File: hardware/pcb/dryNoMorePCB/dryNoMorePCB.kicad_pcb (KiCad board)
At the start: 2 copper layers, 76.2 x 44.2 mm, 34 parts, among them J1 USB_A_Stacked, J10 Barrel_Jack_MountingPin, J11 Conn_01x03, J12 Conn_01x03, J13 Conn_02x06_Odd_Even, J2 Conn_01x03, J3 Conn_01x03, J4 Conn_01x03, J5 USB_A_Stacked, J6 Conn_01x03, J7 Conn_01x03, J8 Conn_01x03, J9 USB_A_Stacked, Q1 Q_NMOS_GDSD, Q2 Q_NMOS_GDSD, Q3 Q_NMOS_GDSD, Q4 Q_NMOS_GDSD, Q5 Q_NMOS_GDSD, Q6 Q_NMOS_GDSD, U1 74HC595, U2 74HC595

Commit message: more routing nightmares incoming
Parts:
- added J14: Conn_02x06_Odd_Even, Connector_PinSocket_2.54mm:PinSocket_2x06_P2.54mm_Horizontal, F.Cu at (77.7, 87.1)
- added J15: Conn_01x02, Connector_PinHeader_2.54mm:PinHeader_1x02_P2.54mm_Vertical, F.Cu at (120.4, 81.5)
- added J16: Conn_01x02, Connector_PinHeader_2.54mm:PinHeader_1x02_P2.54mm_Vertical, F.Cu at (115.0, 81.5)
- added J17: Conn_01x02, Connector_PinHeader_2.54mm:PinHeader_1x02_P2.54mm_Vertical, F.Cu at (107.7, 81.5)
- J13: value Conn_02x06_Odd_Even -> Conn_01x02; footprint Connector_PinSocket_2.54mm:PinSocket_2x06_P2.54mm_Horizontal -> Connector_PinHeader_2.54mm:PinHeader_1x02_P2.54mm_Vertical
- moved J11 20.7 mm to (144.9, 101.3), turned to 180 degrees
- moved Q3 17.2 mm to (131.2, 112.0), turned to 90 degrees
- moved J13 14.6 mm to (91.3, 81.6), turned to 90 degrees
- moved J12 13.9 mm to (144.9, 91.7), turned to 180 degrees
- moved J2 11.0 mm to (139.2, 101.3), turned to 180 degrees
- moved J3 10.0 mm to (131.1, 101.3), turned to 180 degrees
- moved J8 9.63 mm to (131.1, 91.7), turned to 180 degrees
- moved Q5 9.26 mm to (122.2, 111.8)
- moved R5 9.26 mm to (125.8, 105.4)
- moved Q6 9.09 mm to (140.3, 112.0)
- moved R6 9.09 mm to (143.9, 105.6)
- moved R2 9.07 mm to (116.6, 105.4)
- moved Q2 9.07 mm to (113.0, 111.8)
- moved J6 8.84 mm to (135.2, 101.3), turned to 180 degrees
- moved J7 8.47 mm to (139.2, 91.7), turned to 180 degrees
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- renumbered J1 to locked, J9 to locked, J5 to locked
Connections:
- A1 pad 1: unconnected-(A1-Pad1) -> /UNUSED_D_PIN_2
- A1 pad 10: /PWR_CTRL_SHIFT_REG_IN_CLK -> /PWR_CTRL_SHIFT_REG_UPDATE
- A1 pad 11: /PWR_CTRL_SHIFT_REG_UPDATE -> /PWR_CTRL_SHIFT_REG_IN_CLK
- A1 pad 19: /MOIST_SENS_AOUT_1 -> /WAT_LVL_SENS_AOUT_2
- A1 pad 2: unconnected-(A1-Pad2) -> /UNUSED_D_PIN_1
- A1 pad 20: /MOIST_SENS_AOUT_2 -> /WAT_LVL_SENS_AOUT_1
- A1 pad 21: /MOIST_SENS_AOUT_3 -> /MOIST_SENS_AOUT_1
- A1 pad 22: /MOIST_SENS_AOUT_4 -> /MOIST_SENS_AOUT_2
- A1 pad 23: /MOIST_SENS_AOUT_5 -> /MOIST_SENS_AOUT_3
- A1 pad 25: /WAT_LVL_SENS_AOUT_1 -> /MOIST_SENS_AOUT_5
- A1 pad 26: /WAT_LVL_SENS_AOUT_2 -> /MOIST_SENS_AOUT_4
- A1 pad 28: /ETH_RST -> unconnected-(A1-Pad28)
- A1 pad 5: unconnected-(A1-Pad5) -> /UNUSED_D_PIN_3
- A1 pad 6: unconnected-(A1-Pad6) -> /UNUSED_D_PIN_4
- A1 pad 7: unconnected-(A1-Pad7) -> /UNUSED_D_PIN_5
- A1 pad 8: unconnected-(A1-Pad8) -> /UNUSED_D_PIN_6
- J13 pad 1: +5V -> /UNUSED_PWR_CTRL_1
- J13 pad 2: GND -> /UNUSED_PWR_CTRL_2
- U1 pad 1: /WAT_LVL_SENS_PWR_2 -> /MOIST_SENS_PWR_5
- U1 pad 15: /WAT_LVL_SENS_PWR_1 -> /MOIST_SENS_PWR_6
- U1 pad 2: /MOIST_SENS_PWR_6 -> /MOIST_SENS_PWR_4
- U1 pad 6: /MOIST_SENS_PWR_4 -> /WAT_LVL_SENS_PWR_2
- U1 pad 7: /MOIST_SENS_PWR_5 -> /WAT_LVL_SENS_PWR_1
- U2 pad 1: /PUMP_2_CTRL -> /UNUSED_PWR_CTRL_2
- U2 pad 15: /PUMP_1_CTRL -> /UNUSED_PWR_CTRL_1
- U2 pad 2: /PUMP_3_CTRL -> /PUMP_6_CTRL
- U2 pad 3: /PUMP_4_CTRL -> /PUMP_5_CTRL
- U2 pad 4: /PUMP_5_CTRL -> /PUMP_4_CTRL
- U2 pad 5: /PUMP_6_CTRL -> /PUMP_3_CTRL
- U2 pad 6: unconnected-(U2-Pad6) -> /PUMP_2_CTRL
- U2 pad 7: unconnected-(U2-Pad7) -> /PUMP_1_CTRL
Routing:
- net /PUMP_6_CTRL: track 4.08 -> 76.0 mm
- net /PUMP_5_CTRL: track 4.15 -> 66.9 mm
- net /PUMP_4_CTRL: track 4.08 -> 59.3 mm
- net /ETH_RST: track 0.00 -> 51.5 mm
- net /PUMP_3_CTRL: track 4.08 -> 46.5 mm
- net /MOIST_SENS_AOUT_5: track 41.1 -> 0.00 mm
- net /WAT_LVL_SENS_AOUT_2: track 24.2 -> 64.8 mm
- net /MOIST_SENS_AOUT_4: track 40.3 -> 0.00 mm
- net /MOIST_SENS_AOUT_6: track 40.2 -> 0.00 mm
- net /PUMP_2_CTRL: track 4.08 -> 35.2 mm
- net /UNUSED_PWR_CTRL_2: track 0.00 -> 22.3 mm
- net /PUMP_1_CTRL: track 4.08 -> 25.3 mm
- net /WAT_LVL_SENS_AOUT_1: track 30.1 -> 49.4 mm
- net /MOIST_SENS_AOUT_3: track 41.8 -> 26.9 mm
- net /MOIST_SENS_PWR_3: track 27.6 -> 12.9 mm
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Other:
- board size 76.2 x 44.2 mm -> 76.2 x 48.6 mm
- board text added: "J5"
- board text added: "J9"
- board text added: "Q6"

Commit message: almost done with the pcb
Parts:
- added +5V: +5V, Connector_PinHeader_2.54mm:PinHeader_1x02_P2.54mm_Vertical, F.Cu at (91.1, 81.5)
- added +5V: +5V, Connector_PinHeader_2.54mm:PinHeader_1x02_P2.54mm_Vertical, F.Cu at (128.7, 81.5)
- added GND: GND, Connector_PinHeader_2.54mm:PinHeader_1x02_P2.54mm_Vertical, F.Cu at (98.3, 81.5)
- added GND: GND, Connector_PinHeader_2.54mm:PinHeader_1x02_P2.54mm_Vertical, F.Cu at (136.1, 81.5)
- added H1: MountingHole, MountingHole:MountingHole_3.2mm_M3_DIN965, F.Cu at (76.2, 81.4)
- added H2: MountingHole, MountingHole:MountingHole_3.2mm_M3_DIN965, F.Cu at (76.2, 109.2)
- added H3: MountingHole, MountingHole:MountingHole_3.2mm_M3_DIN965, F.Cu at (146.3, 81.4)
- added H4: MountingHole, MountingHole:MountingHole_3.2mm_M3_DIN965, F.Cu at (146.3, 124.0)
- D0 D1: renamed from J15
- D3 D2: renamed from J16
- D4 D5: renamed from J17
- J14: value Conn_02x06_Odd_Even -> ETH_W5500; footprint Connector_PinSocket_2.54mm:PinSocket_2x06_P2.54mm_Horizontal -> Connector_PinHeader_2.54mm:PinHeader_2x05_P2.54mm_Vertical
- PWR 0,7: renamed from J13
- moved R5 9.44 mm to (120.2, 113.0), turned to 90 degrees
- moved R2 9.39 mm to (111.1, 113.0), turned to 90 degrees
- moved R1 9.37 mm to (92.8, 113.0), turned to 90 degrees
- moved R4 9.37 mm to (101.9, 113.0), turned to 90 degrees
- moved R6 9.37 mm to (138.4, 113.2), turned to 90 degrees
- moved R3 9.26 mm to (129.3, 113.0), turned to 90 degrees
- moved PWR 0,7 7.84 mm to (83.4, 81.5)
- moved C1 6.47 mm to (89.2, 93.7), turned to 180 degrees
- moved C4 5.63 mm to (114.4, 93.5), turned to 180 degrees
- moved Q3 5.41 mm to (133.0, 106.8), turned to -90 degrees
- moved Q6 5.34 mm to (142.0, 106.9), turned to -90 degrees
- moved Q2 5.33 mm to (114.7, 106.7), turned to -90 degrees
- moved Q5 5.31 mm to (123.7, 106.7), turned to -90 degrees
- moved Q4 5.29 mm to (105.5, 106.7), turned to -90 degrees
- moved Q1 5.25 mm to (96.3, 106.8), turned to -90 degrees
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- renumbered J2 to S1, J6 to S2, J3 to S3, J7 to S4, J4 to S5, J8 to S6, J11 to W1, J12 to W2
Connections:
- A1 pad 11: /PWR_CTRL_SHIFT_REG_IN_CLK -> /PWR_CTRL_SHIFT_REG_OE
- A1 pad 12: /PWR_CTRL_SHIFT_REG_OE -> /PWR_CTRL
- A1 pad 19: /WAT_LVL_SENS_AOUT_2 -> /WAT_LVL_SENS_AOUT_1
- A1 pad 20: /WAT_LVL_SENS_AOUT_1 -> /WAT_LVL_SENS_AOUT_2
- A1 pad 23: /MOIST_SENS_AOUT_3 -> /MOIST_SENS_AOUT_4
- A1 pad 24: /MOIST_SENS_AOUT_6 -> /MOIST_SENS_AOUT_5
- A1 pad 25: /MOIST_SENS_AOUT_5 -> /MOIST_SENS_AOUT_6
- A1 pad 26: /MOIST_SENS_AOUT_4 -> /MOIST_SENS_AOUT_3
- A1 pad 28: unconnected-(A1-Pad28) -> /ETH_RST
- A1 pad 3: /ETH_RST -> unconnected-(A1-Pad3)
- A1 pad 9: /PWR_CTRL -> /PWR_CTRL_SHIFT_REG_IN_CLK
- J14 pad 1: +5V -> /ETH_SCLK
- J14 pad 10: /ETH_CS -> +5V
- J14 pad 2: GND -> unconnected-(J14-Pad2)
- J14 pad 3: /ETH_INT -> /ETH_CS
- J14 pad 4: /ETH_CLK_OUT -> /ETH_INT
- J14 pad 5: /ETH_MISO -> /ETH_MOSI
- J14 pad 6: /ETH_WAKE_ON_LAN -> /ETH_RST
- J14 pad 7: /ETH_SCLK -> /ETH_MISO
- J14 pad 8: /ETH_MOSI -> GND
- J14 pad 9: /ETH_RST -> +3V3
- U1 pad 1: /MOIST_SENS_PWR_5 -> /WAT_LVL_SENS_PWR_1
- U1 pad 2: /MOIST_SENS_PWR_4 -> /MOIST_SENS_PWR_3
- U1 pad 3: /MOIST_SENS_PWR_1 -> /MOIST_SENS_PWR_2
- U1 pad 4: /MOIST_SENS_PWR_2 -> /MOIST_SENS_PWR_1
- U1 pad 5: /MOIST_SENS_PWR_3 -> /MOIST_SENS_PWR_5
- U1 pad 6: /WAT_LVL_SENS_PWR_2 -> /MOIST_SENS_PWR_4
- U1 pad 7: /WAT_LVL_SENS_PWR_1 -> /WAT_LVL_SENS_PWR_2
- U2 pad 1: /UNUSED_PWR_CTRL_2 -> /PUMP_1_CTRL
- U2 pad 7: /PUMP_1_CTRL -> /UNUSED_PWR_CTRL_2
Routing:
- net /MOIST_SENS_AOUT_4: track 0.00 -> 45.9 mm
- net /MOIST_SENS_AOUT_5: track 0.00 -> 42.6 mm
- net /MOIST_SENS_AOUT_6: track 0.00 -> 42.5 mm
- net +5V: track 0.00 -> 28.1 mm, vias 0 -> 4
- net /PUMP_2_CTRL: track 35.2 -> 18.9 mm
- net /PUMP_4_PWR: track 0.00 -> 15.8 mm
- net /PUMP_2_PWR: track 0.00 -> 15.7 mm
- net /WAT_LVL_SENS_PWR_1: track 22.5 -> 38.0 mm
- net /PUMP_6_PWR: track 0.00 -> 15.4 mm
- net /PUMP_3_CTRL: track 46.5 -> 32.2 mm
- net /MOIST_SENS_PWR_5: track 35.1 -> 21.1 mm
- net /PUMP_4_CTRL: track 59.3 -> 45.5 mm
- net /ETH_SCLK: track 12.4 -> 24.0 mm
- net /MOIST_SENS_PWR_6: track 21.2 -> 31.8 mm
- net /MOIST_SENS_PWR_4: track 33.2 -> 22.7 mm
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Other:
- outline, holes or cut-outs redrawn
- board text added: "+"
- board text added: "+3V"
- board text added: "+5V"
- board text added: "-"
- board text added: "0.1µF"
- board text added: "1µF"
- board text added: "<- Arduino USB port direction"
- board text added: "C1"
- board text added: "C2"
- board text added: "C4"
- board text added: "C5"
- board text added: "DryNoMore v0.1"
- board text added: "GND"
- board text added: "Moisture sensors"
- board text added: "USB pumps Top: P2|P4|P6 Bot: P1|P3|P5"
- board text added: "Waterlevel sensors"
- board text added: "by 7FM"
- board text removed: "J5"
- board text removed: "J9"
- board text removed: "Q6"

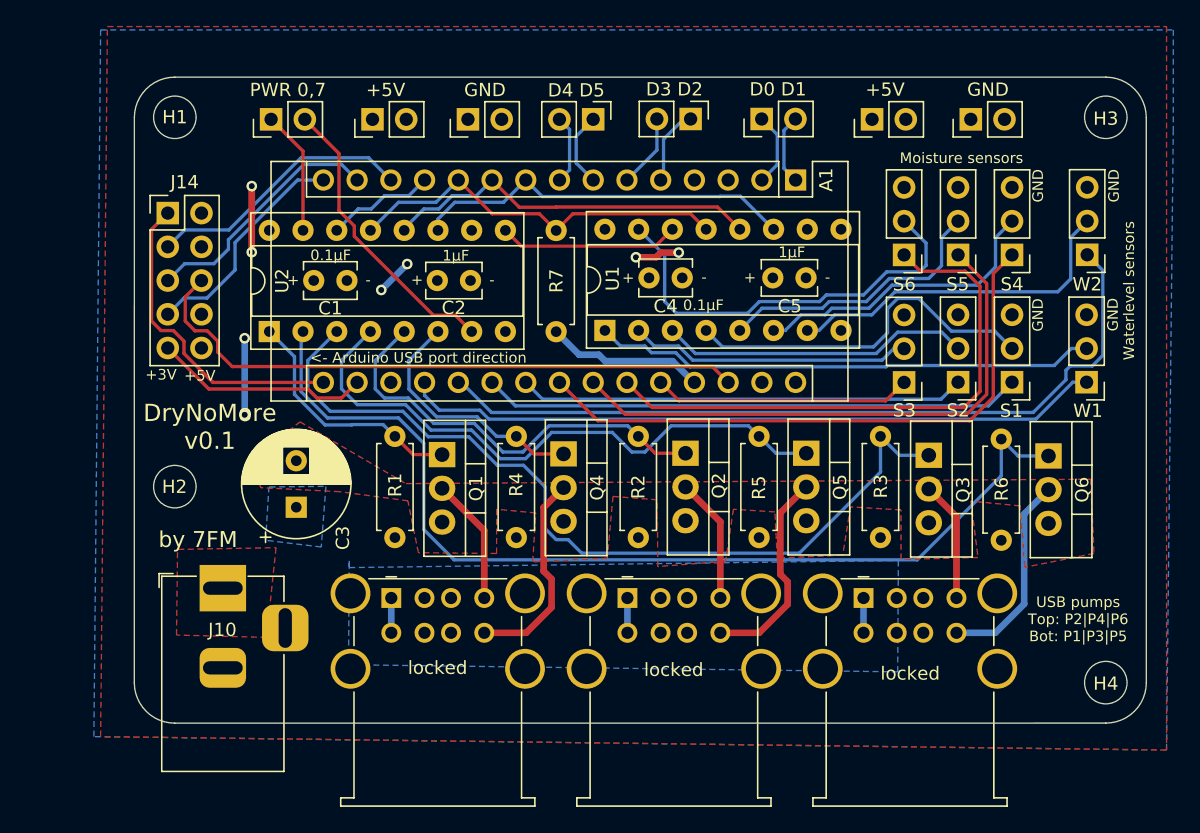
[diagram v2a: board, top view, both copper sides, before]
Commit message: eth W5500: only connect 5V, add circuit tree icon to the backside
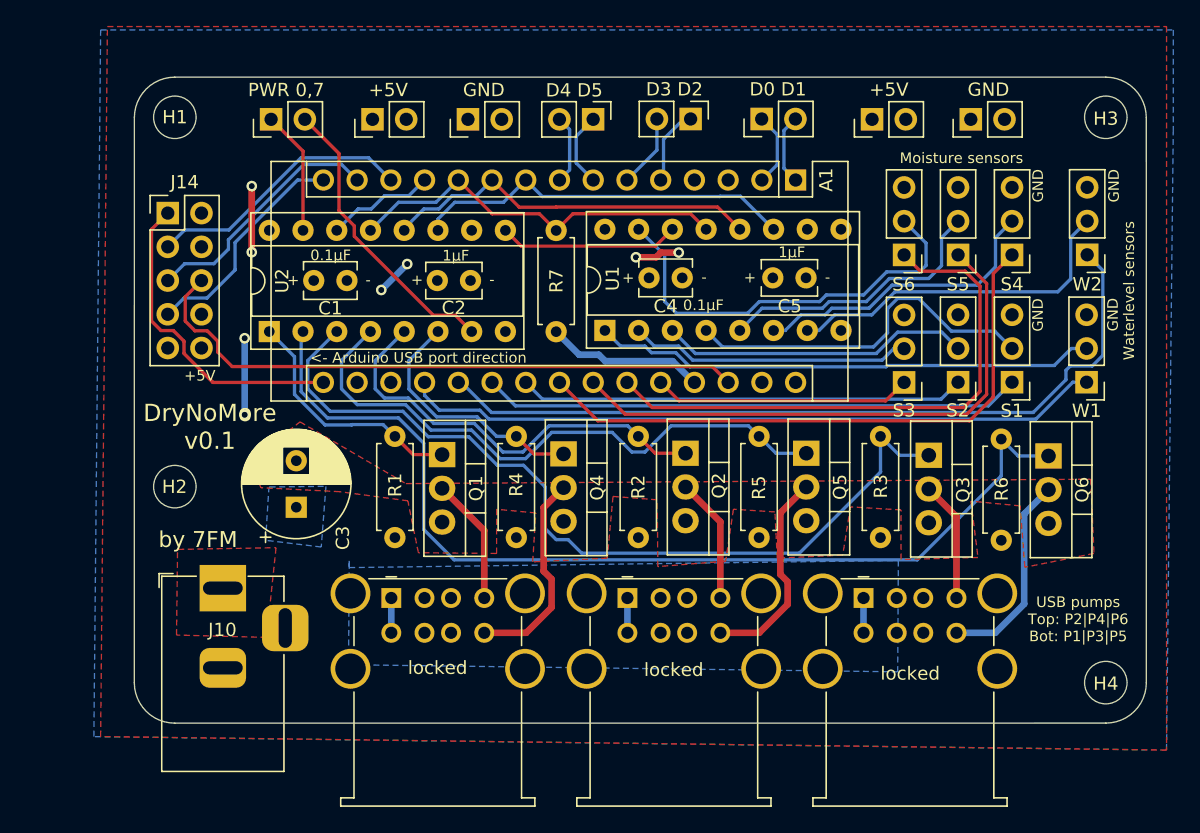
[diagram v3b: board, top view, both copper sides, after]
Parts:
- added G***: LOGO, icon:icon, B.Cu at (111.4, 103.0)
- J13: renamed from PWR 0,7
- J15: renamed from D0 D1
- J16: renamed from D3 D2
- J17: renamed from D4 D5
- renumbered W1 to J11, W2 to J12, GND to J18, GND to J19, S1 to J2, +5V to J20, +5V to J21, S3 to J3, S5 to J4, S2 to J6, S4 to J7, S6 to J8
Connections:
- J14 pad 9: +3V3 -> unconnected-(J14-Pad9)
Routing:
- net +3V3: track 16.3 -> 0.00 mm
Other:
- board text added: "D0 D1"
- board text added: "D3 D2"
- board text added: "D4 D5"
- board text added: "Img source: vecteezy.com"
- board text added: "PWR 0,7"
- board text added: "S1"
- board text added: "S2"
- board text added: "S3"
- board text added: "S4"
- board text added: "S5"
- board text added: "S6"
- board text added: "W1"
- board text added: "W2"
- board text removed: "+3V"

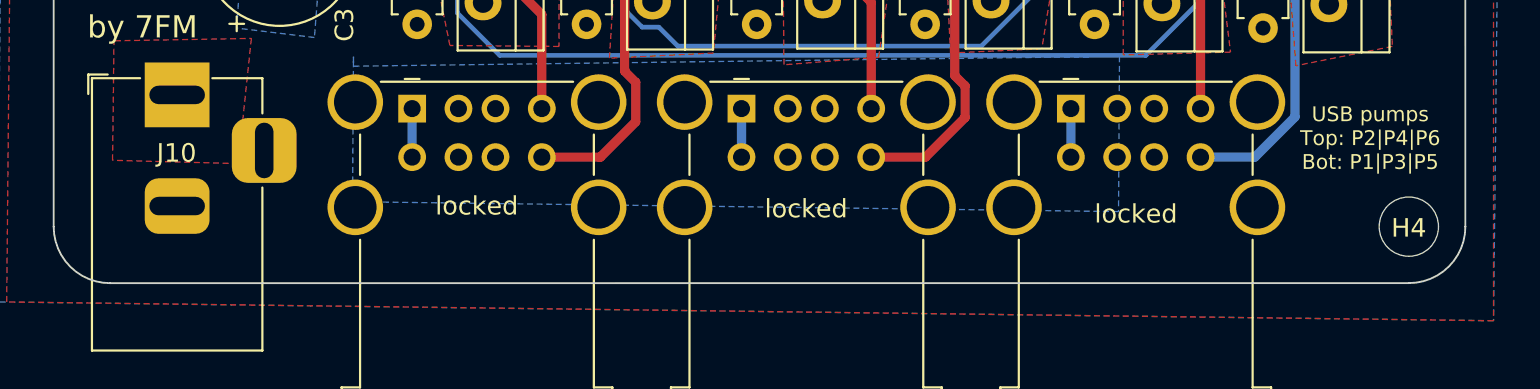
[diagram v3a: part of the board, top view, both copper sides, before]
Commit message: fix missing filling +5V zone, USB pump silkscreen numbering
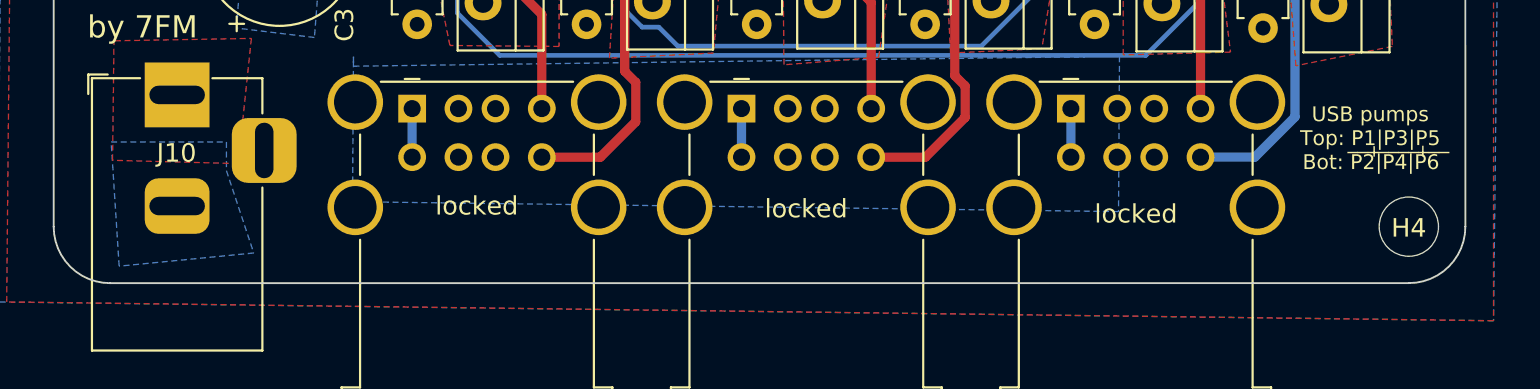
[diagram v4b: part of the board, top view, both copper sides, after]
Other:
- board text added: "Bot: P2|P4|P6"
- board text added: "USB pumps Top: P1|P3|P5"
- board text added: "_"
- board text added: "__________"
- board text removed: "USB pumps Top: P2|P4|P6 Bot: P1|P3|P5"
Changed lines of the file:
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@@
+    (effects (font (size 0.8 0.8) (thickness 0.1)))
+  )
+  (gr_text "_" (at 146.47 119.87 90) (layer "F.SilkS")
     (effects (font (size 0.8 0.8) (thickness 0.1)))
   )
@@
   )
   (gr_text "1µF" (at 97.3582 91.7956) (layer "F.SilkS")
+    (effects (font (size 0.8 0.8) (thickness 0.1)))
+  )
+  (gr_text "__________" (at 145.74 119.36) (layer "F.SilkS")
     (effects (font (size 0.8 0.8) (thickness 0.1)))
   )
@@
     (effects (font (size 0.8 0.8) (thickness 0.1)))
   )
-  (gr_text "USB pumps\nTop: P2|P4|P6\nBot: P1|P3|P5" (at 144.2212 119.1768) (layer "F.SilkS")
+  (gr_text "USB pumps\nTop: P1|P3|P5\n " (at 144.2212 119.1768) (layer "F.SilkS")
     (effects (font (size 0.8 0.8) (thickness 0.1)))
   )
@@
   )
   (gr_text "-" (at 100.076 93.599) (layer "F.SilkS")
+    (effects (font (size 0.8 0.8) (thickness 0.1)))
+  )
+  (gr_text "_" (at 145.02 119.89 270) (layer "F.SilkS")
+    (effects (font (size 0.8 0.8) (thickness 0.1)))
+  )
+  (gr_text "Bot: P2|P4|P6" (at 144.26 120.4722) (layer "F.SilkS")
     (effects (font (size 0.8 0.8) (thickness 0.1)))
   )
@@
     )
   )
+  (zone (net 26) (net_name "+5V") (layer "B.Cu") (hatch edge 0.508)
+    (connect_pads (clearance 0.508))
+    (min_thickness 0.254) (filled_areas_thickness no)
+    (fill yes (thermal_gap 0.508) (thermal_bridge_width 2))
+    (polygon
+      (pts
+        (xy 82.4738 120.9294)
+        (xy 83.947 125.3744)
+        (xy 76.6826 126.0856)
+        (xy 76.2508 119.38)
+        (xy 82.4738 119.38)
+      )
+    )
+  )
+  (group "" (id 0b73c48d-b969-4f2d-8b6f-1224277ec2cf)
+    (members
+      029f3c7b-7531-4f07-9362-9c03d1ed7a09
+      46072e56-672e-4134-9035-1ab62b6d53d1
+      97f2a5a8-92c9-4279-8401-839bb9c840c6
+      c4194f32-cac3-4cfb-a6b9-3e763933b819
+      e19299b4-371c-4d75-9517-7446b6e330fb
+    )
+  )
